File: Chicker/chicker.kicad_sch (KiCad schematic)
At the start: 0 parts

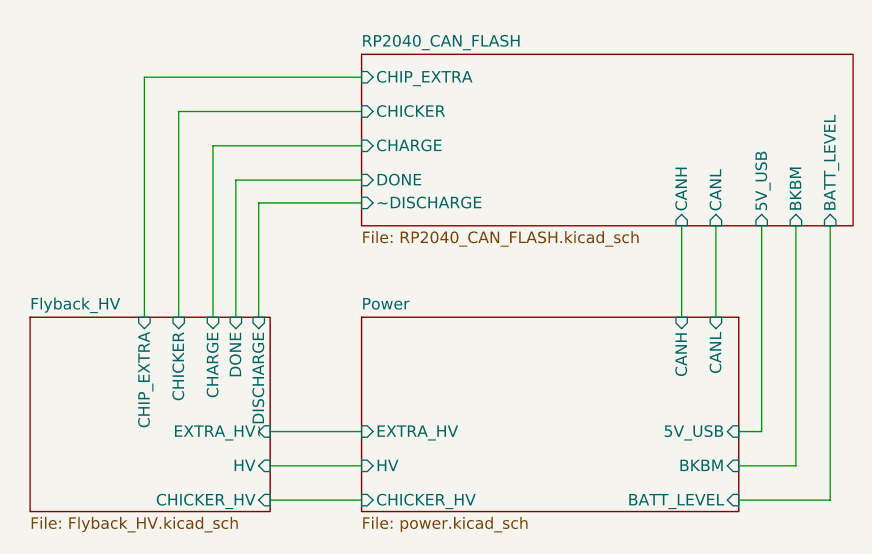
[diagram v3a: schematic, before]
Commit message: chicker discharge circuit finalized
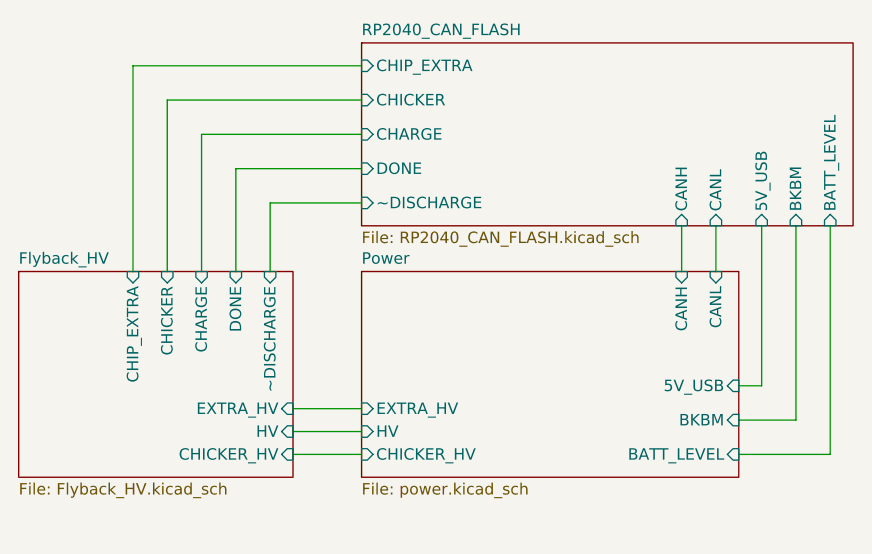
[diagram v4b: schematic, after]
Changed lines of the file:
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@@
 (kicad_sch (version 20230121) (generator eeschema)
   (paper "A5")
-  (wire (pts (xy 139.7 77.47) (xy 146.05 77.47))
+  (wire (pts (xy 139.7 72.39) (xy 146.05 72.39))
     (stroke (width 0) (type default))
   )
-  (wire (pts (xy 142.24 73.66) (xy 139.7 73.66))
+  (wire (pts (xy 142.24 68.58) (xy 139.7 68.58))
     (stroke (width 0) (type default))
   )
-  (wire (pts (xy 97.79 48.26) (xy 86.36 48.26))
+  (wire (pts (xy 97.79 48.26) (xy 87.63 48.26))
     (stroke (width 0) (type default))
   )
-  (wire (pts (xy 97.79 38.1) (xy 77.47 38.1))
+  (wire (pts (xy 97.79 36.83) (xy 76.2 36.83))
     (stroke (width 0) (type default))
   )
-  (wire (pts (xy 142.24 50.8) (xy 142.24 73.66))
+  (wire (pts (xy 90.17 73.66) (xy 97.79 73.66))
     (stroke (width 0) (type default))
   )
-  (wire (pts (xy 149.86 81.28) (xy 149.86 50.8))
+  (wire (pts (xy 142.24 50.8) (xy 142.24 68.58))
     (stroke (width 0) (type default))
   )
-  (wire (pts (xy 139.7 81.28) (xy 149.86 81.28))
+  (wire (pts (xy 149.86 76.2) (xy 149.86 50.8))
     (stroke (width 0) (type default))
   )
-  (wire (pts (xy 133.35 50.8) (xy 133.35 60.96))
+  (wire (pts (xy 139.7 76.2) (xy 149.86 76.2))
     (stroke (width 0) (type default))
   )
-  (wire (pts (xy 86.36 48.26) (xy 86.36 60.96))
+  (wire (pts (xy 133.35 50.8) (xy 133.35 55.88))
     (stroke (width 0) (type default))
   )
-  (wire (pts (xy 87.63 81.28) (xy 97.79 81.28))
+  (wire (pts (xy 87.63 48.26) (xy 87.63 55.88))
     (stroke (width 0) (type default))
   )
-  (wire (pts (xy 81.28 41.91) (xy 97.79 41.91))
+  (wire (pts (xy 80.01 40.64) (xy 97.79 40.64))
     (stroke (width 0) (type default))
   )
-  (wire (pts (xy 81.28 60.96) (xy 81.28 41.91))
+  (wire (pts (xy 80.01 55.88) (xy 80.01 40.64))
     (stroke (width 0) (type default))
   )
-  (wire (pts (xy 97.79 45.72) (xy 83.82 45.72))
+  (wire (pts (xy 97.79 44.45) (xy 83.82 44.45))
     (stroke (width 0) (type default))
   )
-  (wire (pts (xy 97.79 34.29) (xy 73.66 34.29))
+  (wire (pts (xy 97.79 33.02) (xy 72.39 33.02))
     (stroke (width 0) (type default))
   )
-  (wire (pts (xy 87.63 73.66) (xy 97.79 73.66))
+  (wire (pts (xy 90.17 71.12) (xy 97.79 71.12))
     (stroke (width 0) (type default))
   )
-  (wire (pts (xy 87.63 77.47) (xy 97.79 77.47))
+  (wire (pts (xy 90.17 76.2) (xy 97.79 76.2))
     (stroke (width 0) (type default))
   )
-  (wire (pts (xy 146.05 77.47) (xy 146.05 50.8))
+  (wire (pts (xy 146.05 72.39) (xy 146.05 50.8))
     (stroke (width 0) (type default))
   )
-  (wire (pts (xy 83.82 45.72) (xy 83.82 60.96))
+  (wire (pts (xy 83.82 44.45) (xy 83.82 55.88))
     (stroke (width 0) (type default))
   )
-  (wire (pts (xy 137.16 50.8) (xy 137.16 60.96))
+  (wire (pts (xy 137.16 50.8) (xy 137.16 55.88))
     (stroke (width 0) (type default))
   )
-  (wire (pts (xy 73.66 34.29) (xy 73.66 60.96))
+  (wire (pts (xy 72.39 33.02) (xy 72.39 55.88))
     (stroke (width 0) (type default))
   )
-  (wire (pts (xy 77.47 38.1) (xy 77.47 60.96))
+  (wire (pts (xy 76.2 36.83) (xy 76.2 55.88))
     (stroke (width 0) (type default))
   )
-  (sheet (at 97.79 60.96) (size 41.91 21.59) (fields_autoplaced)
+  (sheet (at 97.79 55.88) (size 41.91 22.86) (fields_autoplaced)
     (stroke (width 0.1524) (type solid))
     (fill (color 0 0 0 0.0000))
-    (property "Sheetname" "Power" (at 97.79 60.2484 0)
+    (property "Sheetname" "Power" (at 97.79 55.1684 0)
       (effects (font (size 1.27 1.27)) (justify left bottom))
     )
-    (property "Sheetfile" "power.kicad_sch" (at 97.79 83.1346 0)
+    (property "Sheetfile" "power.kicad_sch" (at 97.79 79.3246 0)
       (effects (font (size 1.27 1.27)) (justify left top))
     )
-    (pin "CANL" input (at 137.16 60.96 90)
+    (pin "CANL" input (at 137.16 55.88 90)
       (effects (font (size 1.27 1.27)) (justify right))
     )
-    (pin "CHICKER_HV" input (at 97.79 81.28 180)
+    (pin "CHICKER_HV" input (at 97.79 76.2 180)
       (effects (font (size 1.27 1.27)) (justify left))
     )
-    (pin "BKBM" input (at 139.7 77.47 0)
+    (pin "BKBM" input (at 139.7 72.39 0)
       (effects (font (size 1.27 1.27)) (justify right))
     )
-    (pin "HV" input (at 97.79 77.47 180)
+    (pin "HV" input (at 97.79 73.66 180)
       (effects (font (size 1.27 1.27)) (justify left))
     )
-    (pin "EXTRA_HV" input (at 97.79 73.66 180)
+    (pin "EXTRA_HV" input (at 97.79 71.12 180)
       (effects (font (size 1.27 1.27)) (justify left))
     )
-    (pin "CANH" input (at 133.35 60.96 90)
+    (pin "CANH" input (at 133.35 55.88 90)
       (effects (font (size 1.27 1.27)) (justify right))
     )
-    (pin "5V_USB" input (at 139.7 73.66 0)
+    (pin "5V_USB" input (at 139.7 68.58 0)
       (effects (font (size 1.27 1.27)) (justify right))
     )
-    (pin "BATT_LEVEL" input (at 139.7 81.28 0)
+    (pin "BATT_LEVEL" input (at 139.7 76.2 0)
       (effects (font (size 1.27 1.27)) (justify right))
     )
@@
     )
   )
-  (sheet (at 97.79 31.75) (size 54.61 19.05) (fields_autoplaced)
+  (sheet (at 97.79 30.48) (size 54.61 20.32) (fields_autoplaced)
     (stroke (width 0.1524) (type solid))
     (fill (color 0 0 0 0.0000))
-    (property "Sheetname" "RP2040_CAN_FLASH" (at 97.79 31.0384 0)
+    (property "Sheetname" "RP2040_CAN_FLASH" (at 97.79 29.7684 0)
       (effects (font (size 1.27 1.27)) (justify left bottom))
     )
@@
       (effects (font (size 1.27 1.27)) (justify left))
     )
-    (pin "DONE" input (at 97.79 45.72 180)
+    (pin "DONE" input (at 97.79 44.45 180)
       (effects (font (size 1.27 1.27)) (justify left))
     )
-    (pin "CHICKER" input (at 97.79 38.1 180)
+    (pin "CHICKER" input (at 97.79 36.83 180)
       (effects (font (size 1.27 1.27)) (justify left))
     )
-    (pin "CHIP_EXTRA" input (at 97.79 34.29 180)
+    (pin "CHIP_EXTRA" input (at 97.79 33.02 180)
       (effects (font (size 1.27 1.27)) (justify left))
     )
-    (pin "CHARGE" input (at 97.79 41.91 180)
+    (pin "CHARGE" input (at 97.79 40.64 180)
       (effects (font (size 1.27 1.27)) (justify left))
     )
@@
     )
   )
-  (sheet (at 60.96 60.96) (size 26.67 21.59) (fields_autoplaced)
+  (sheet (at 59.69 55.88) (size 30.48 22.86) (fields_autoplaced)
     (stroke (width 0.1524) (type solid))
     (fill (color 0 0 0 0.0000))
-    (property "Sheetname" "Flyback_HV" (at 60.96 60.2484 0)
+    (property "Sheetname" "Flyback_HV" (at 59.69 55.1684 0)
       (effects (font (size 1.27 1.27)) (justify left bottom))
     )
-    (property "Sheetfile" "Flyback_HV.kicad_sch" (at 60.96 83.1346 0)
+    (property "Sheetfile" "Flyback_HV.kicad_sch" (at 59.69 79.3246 0)
       (effects (font (size 1.27 1.27)) (justify left top))
     )
-    (pin "CHICKER" input (at 77.47 60.96 90)
+    (pin "CHICKER" input (at 76.2 55.88 90)
       (effects (font (size 1.27 1.27)) (justify right))
     )
-    (pin "CHIP_EXTRA" input (at 73.66 60.96 90)
+    (pin "CHIP_EXTRA" input (at 72.39 55.88 90)
       (effects (font (size 1.27 1.27)) (justify right))
     )
-    (pin "CHARGE" input (at 81.28 60.96 90)
+    (pin "CHARGE" input (at 80.01 55.88 90)
       (effects (font (size 1.27 1.27)) (justify right))
     )
-    (pin "DONE" input (at 83.82 60.96 90)
+    (pin "DONE" input (at 83.82 55.88 90)
       (effects (font (size 1.27 1.27)) (justify right))
     )
-    (pin "HV" input (at 87.63 77.47 0)
+    (pin "HV" input (at 90.17 73.66 0)
       (effects (font (size 1.27 1.27)) (justify right))
     )
-    (pin "CHICKER_HV" input (at 87.63 81.28 0)
+    (pin "CHICKER_HV" input (at 90.17 76.2 0)
       (effects (font (size 1.27 1.27)) (justify right))
     )
-    (pin "EXTRA_HV" input (at 87.63 73.66 0)
+    (pin "EXTRA_HV" input (at 90.17 71.12 0)
       (effects (font (size 1.27 1.27)) (justify right))
     )
-    (pin "~DISCHARGE" input (at 86.36 60.96 90)
+    (pin "~DISCHARGE" input (at 87.63 55.88 90)
       (effects (font (size 1.27 1.27)) (justify right))
     )

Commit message: chicker updates
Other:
- added sheet High Voltage Feedback (HV-feedback.kicad_sch)
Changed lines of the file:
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@@
+    )
+  )
+  (sheet (at 160.02 30.48) (size 19.05 19.05) (fields_autoplaced)
+    (stroke (width 0.1524) (type solid))
+    (fill (color 0 0 0 0.0000))
+    (property "Sheetname" "High Voltage Feedback" (at 160.02 29.7684 0)
+      (effects (font (size 1.27 1.27)) (justify left bottom))
+    )
+    (property "Sheetfile" "HV-feedback.kicad_sch" (at 160.02 50.1146 0)
+      (effects (font (size 1.27 1.27)) (justify left top))
+    )
+    (instances
+      (project "chicker"
+        (path "/1a9ce3e8-a091-496c-9c5f-e7b2eb60e275" (page "5"))
+      )
     )
   )

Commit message: chicker v1.1 updates
nearly done, need to fix rules
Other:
- sheet High Voltage Feedback ports: added HV, HV_SENSE; removed none
- sheet Power ports: added 5V_LEVEL; removed none
- sheet RP2040_CAN_FLASH ports: added 5V_LEVEL, HV_SENSE; removed none

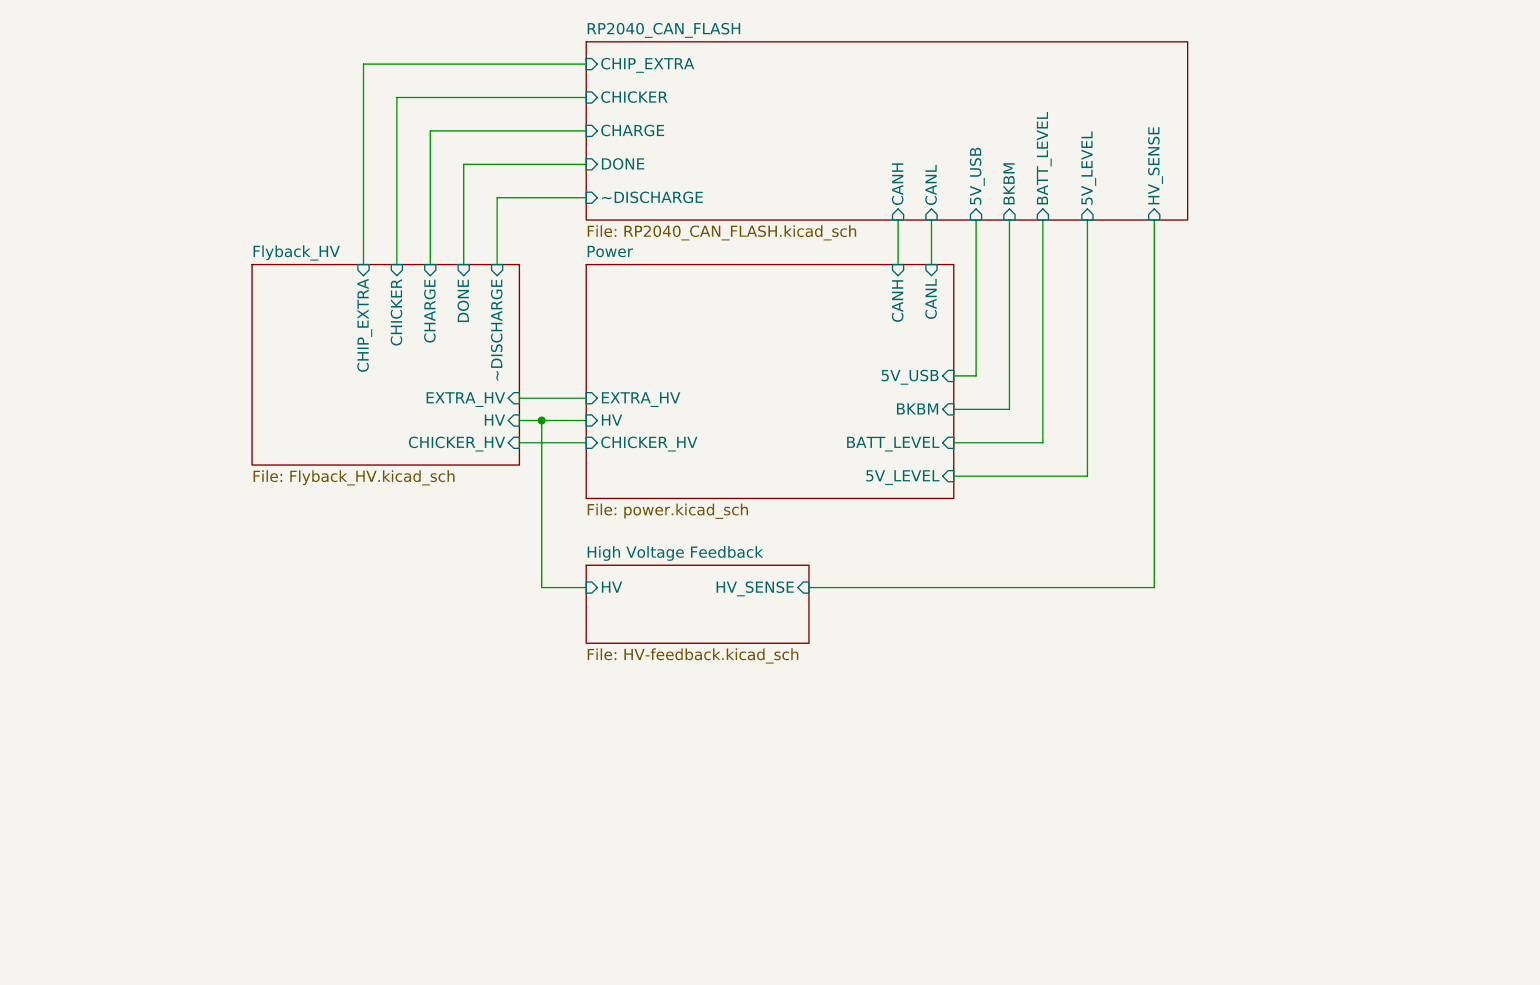
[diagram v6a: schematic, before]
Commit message: v1.1 mostly done, need to add tooling holes
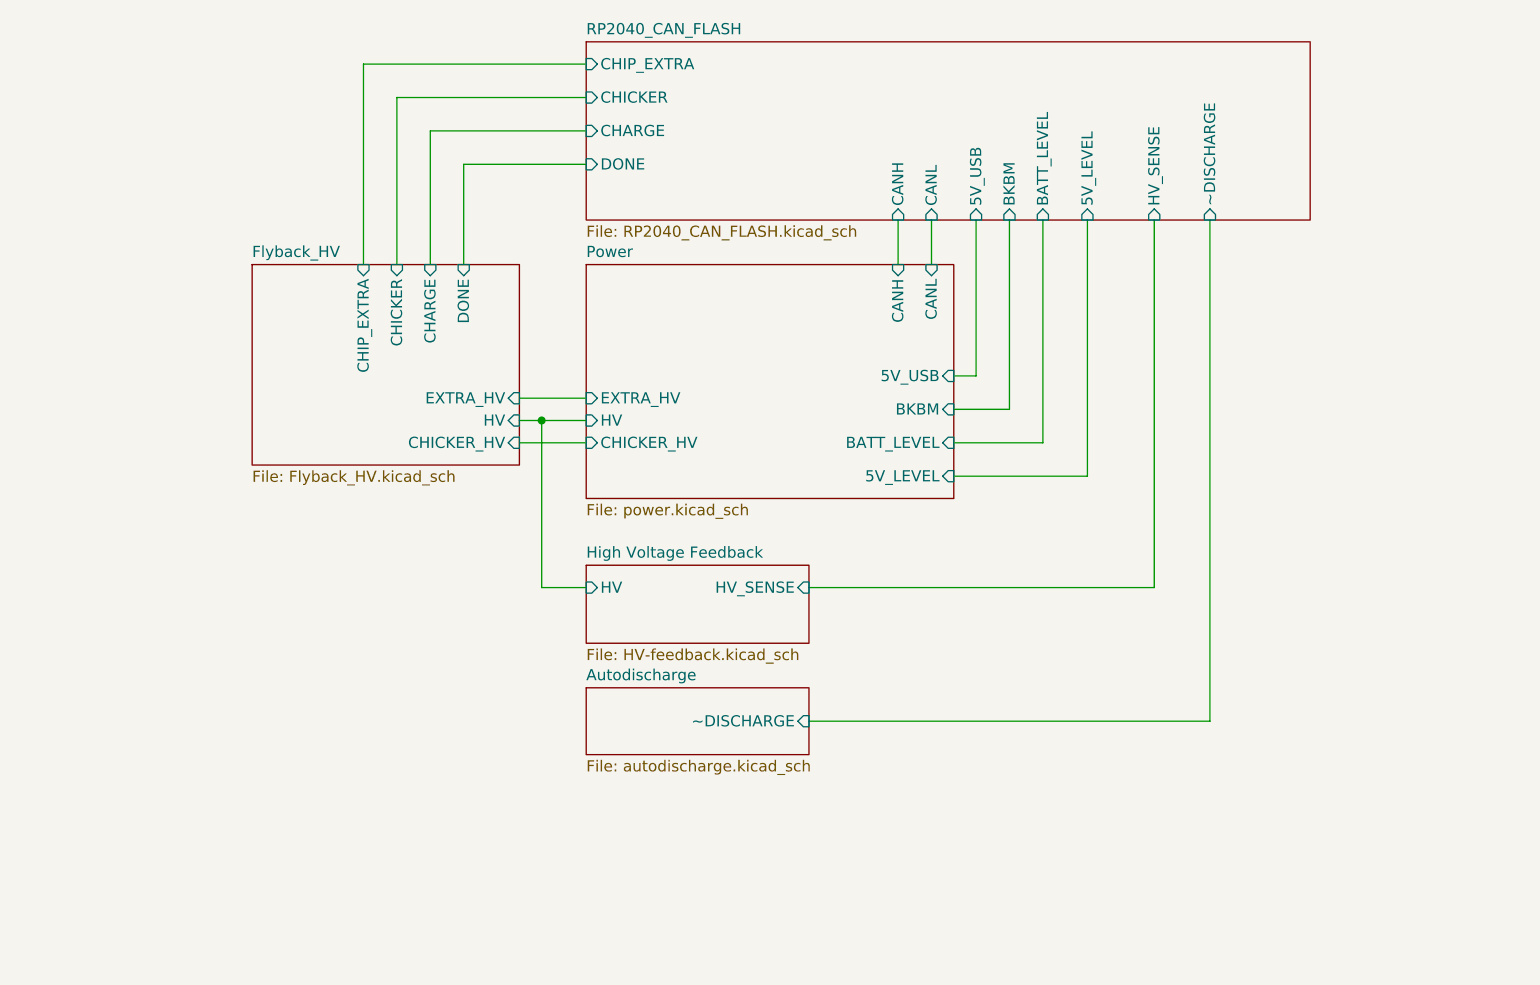
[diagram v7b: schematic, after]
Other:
- added sheet Autodischarge (autodischarge.kicad_sch)
- sheet Flyback_HV ports: added none; removed ~DISCHARGE
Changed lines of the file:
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@@
     (stroke (width 0) (type default))
   )
-  (wire (pts (xy 96.52 38.1) (xy 86.36 38.1))
+  (wire (pts (xy 121.92 97.79) (xy 167.64 97.79))
     (stroke (width 0) (type default))
   )
@@
     (stroke (width 0) (type default))
   )
-  (wire (pts (xy 86.36 38.1) (xy 86.36 45.72))
+  (wire (pts (xy 167.64 40.64) (xy 167.64 97.79))
     (stroke (width 0) (type default))
   )
@@
     )
   )
-  (sheet (at 96.52 20.32) (size 68.58 20.32) (fields_autoplaced)
+  (sheet (at 96.52 93.98) (size 25.4 7.62) (fields_autoplaced)
+    (stroke (width 0.1524) (type solid))
+    (fill (color 0 0 0 0.0000))
+    (property "Sheetname" "Autodischarge" (at 96.52 93.2684 0)
+      (effects (font (size 1.27 1.27)) (justify left bottom))
+    )
+    (property "Sheetfile" "autodischarge.kicad_sch" (at 96.52 102.1846 0)
+      (effects (font (size 1.27 1.27)) (justify left top))
+    )
+    (pin "~DISCHARGE" input (at 121.92 97.79 0)
+      (effects (font (size 1.27 1.27)) (justify right))
+    )
+    (instances
+      (project "chicker"
+        (path "/1a9ce3e8-a091-496c-9c5f-e7b2eb60e275" (page "6"))
+      )
+    )
+  )
+  (sheet (at 96.52 20.32) (size 82.55 20.32) (fields_autoplaced)
     (stroke (width 0.1524) (type solid))
     (fill (color 0 0 0 0.0000))
@@
       (effects (font (size 1.27 1.27)) (justify left))
     )
-    (pin "~DISCHARGE" input (at 96.52 38.1 180)
+    (pin "~DISCHARGE" input (at 167.64 40.64 270)
       (effects (font (size 1.27 1.27)) (justify left))
     )
@@
       (effects (font (size 1.27 1.27)) (justify right))
     )
-    (pin "~DISCHARGE" input (at 86.36 45.72 90)
-      (effects (font (size 1.27 1.27)) (justify right))
-    )

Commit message: chicker modifications (mostly ready to order)
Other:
- sheet Flyback_HV ports: added CHIP, CHIP_HV, KICK, KICK_HV; removed CHICKER, CHICKER_HV, CHIP_EXTRA, EXTRA_HV
- sheet Power ports: added CHIP_HV, KICK_HV; removed CHICKER_HV, EXTRA_HV
- sheet RP2040_CAN_FLASH ports: added CHIP, KICK; removed CHICKER, CHIP_EXTRA
